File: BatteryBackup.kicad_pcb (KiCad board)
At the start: 2 copper layers, 49 x 32 mm, 16 parts, among them J1 Power, J2 Power, J3 PowerOut, Q1 FDMT800100DC, Q2 FDMT800100DC, U1 LTC4357DCB, U2 LTC4357DCB

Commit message: routet
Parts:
- moved R2 15.2 mm to (137.0, 70.7)
- moved C4 15.2 mm to (139.0, 70.8)
- moved R1 13.8 mm to (145.7, 82.7)
- moved C3 13.7 mm to (144.0, 82.7)
- moved U1 10.4 mm to (141.7, 86.4), turned to 90 degrees
- moved U2 8.81 mm to (141.7, 73.4), turned to 90 degrees
- moved Q1 1.50 mm to (148.5, 88.8), turned to 0 degrees
- moved Q2 0.50 mm to (148.0, 74.2), turned to 0 degrees
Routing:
- net /IdealDiode/Vout: track 0.00 -> 85.8 mm, vias 0 -> 2
- net /IdealDiode1/Vin: track 0.00 -> 13.1 mm
- net /IdealDiode/Vin: track 0.00 -> 12.1 mm
- net GND: track 0.00 -> 12.0 mm, vias 0 -> 9
- net Net-(U1-Vdd): track 0.00 -> 6.21 mm
- net Net-(Q2-G): track 0.00 -> 4.51 mm
- net Net-(U2-Vdd): track 0.00 -> 4.34 mm
- net Net-(Q1-G): track 0.00 -> 3.26 mm
- added copper zone on B.Cu, net GND

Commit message: cooling
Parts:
- moved R2 5.09 mm to (141.6, 68.5), turned to 180 degrees
- moved C4 2.64 mm to (141.5, 70.0), turned to 0 degrees
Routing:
- net /IdealDiode/Vout: track 85.8 -> 30.4 mm
- net Net-(U2-Vdd): track 4.34 -> 3.64 mm
- net GND: track 12.0 -> 12.5 mm, vias 9 -> 8
- added copper zone on F.Cu, net /IdealDiode/Vout

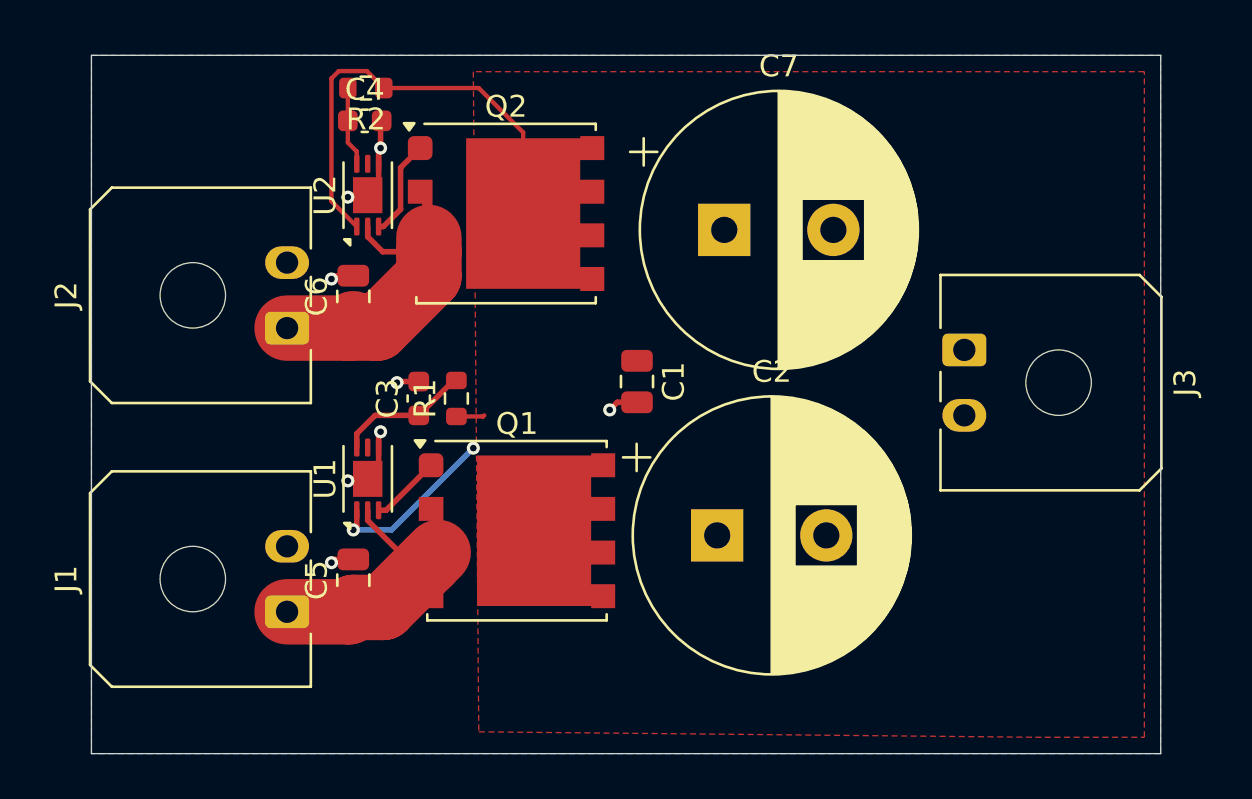
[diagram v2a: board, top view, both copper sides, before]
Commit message: skiftet til LTC4359
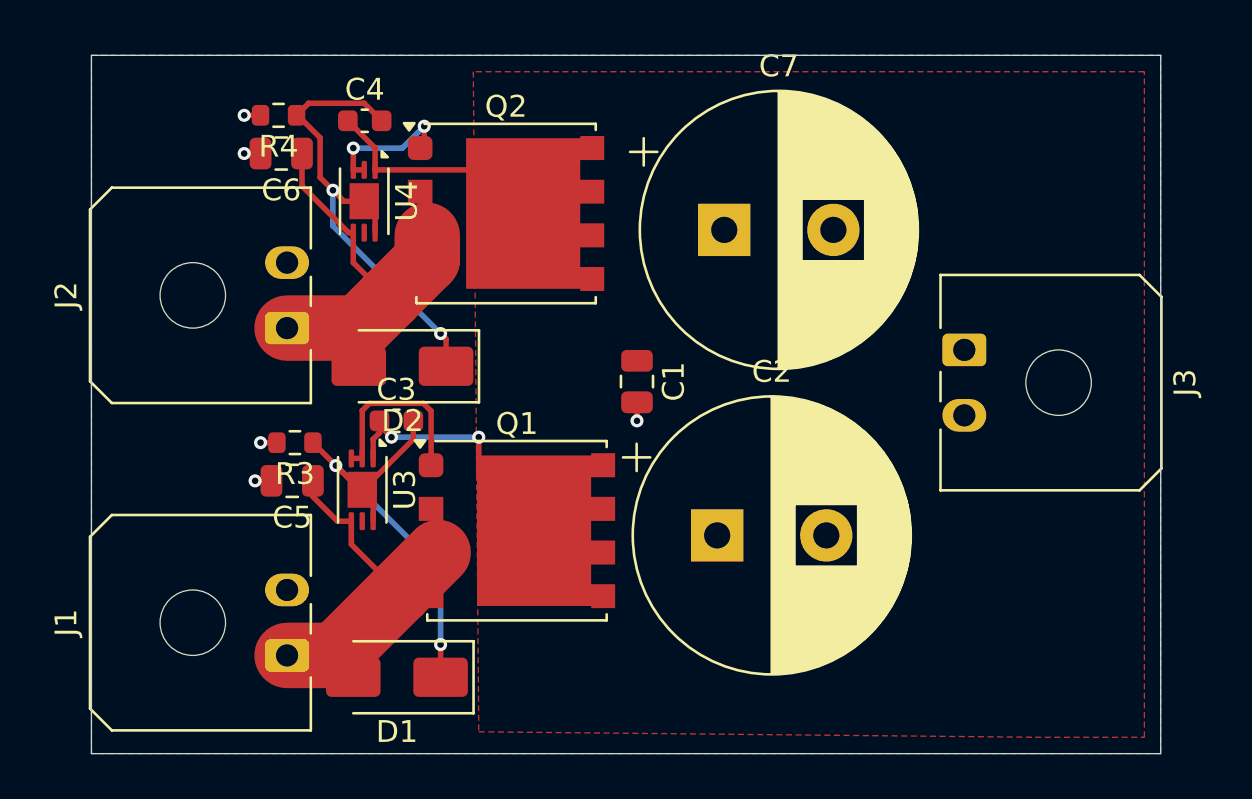
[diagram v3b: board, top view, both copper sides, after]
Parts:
- removed R1, R2: 100, Resistor_SMD:R_0603_1608Metric
- removed U1, U2: LTC4357DCB, Package_DFN_QFN:DFN-6-1EP_3x2mm_P0.5mm_EP1.65x1.35mm
- added D1: SMAJ24CA, Diode_SMD:D_SMA, F.Cu at (143.0, 95.5)
- added D2: SMAJ24CA, Diode_SMD:D_SMA, F.Cu at (143.2, 81.2)
- added R3: 1k, Resistor_SMD:R_0603_1608Metric, F.Cu at (138.3, 84.8)
- added R4: 1k, Resistor_SMD:R_0603_1608Metric, F.Cu at (137.6, 69.8)
- added U3: LTC4359-DCB, Package_DFN_QFN:DFN-6-1EP_3x2mm_P0.5mm_EP1.65x1.35mm, F.Cu at (141.4, 86.9)
- added U4: LTC4359-DCB, Package_DFN_QFN:DFN-6-1EP_3x2mm_P0.5mm_EP1.65x1.35mm, F.Cu at (141.5, 73.7)
- C3, C4: value 100n -> 1,5uF
- moved C6 7.33 mm to (137.7, 71.5), turned to 180 degrees
- moved C5 5.34 mm to (138.2, 86.5), turned to 180 degrees
- moved J1 2.00 mm to (138.0, 94.5)
- moved C3 1.45 mm to (143.0, 83.8), turned to 0 degrees
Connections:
- C3 pad 1: Net-(U1-Vdd) -> /IdealDiode/Vout
- C3 pad 2: GND -> Net-(D1-A1)
- C4 pad 1: Net-(U2-Vdd) -> /IdealDiode/Vout
- C4 pad 2: GND -> Net-(D2-A1)
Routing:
- net Net-(D2-A1): track 0.00 -> 22.1 mm, vias 0 -> 2
- net Net-(D1-A1): track 0.00 -> 20.6 mm, vias 0 -> 2
- net GND: track 12.5 -> 3.85 mm, vias 8 -> 5
- net /IdealDiode/Vout: track 30.4 -> 22.5 mm
- net Net-(U1-Vdd): track 6.21 -> 0.00 mm
- net Net-(Q1-G): track 3.26 -> 8.62 mm
- net /IdealDiode1/Vin: track 13.1 -> 17.2 mm
- net /IdealDiode/Vin: track 12.1 -> 16.0 mm
- net Net-(U2-Vdd): track 3.64 -> 0.00 mm
- net Net-(Q2-G): track 4.51 -> 6.24 mm, vias 0 -> 2

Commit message: fejlretning
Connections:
- U3 pad 3: Net-(Q1-G) -> /IdealDiode/Vin
- U4 pad 3: Net-(Q2-G) -> /IdealDiode1/Vin
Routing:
- net /IdealDiode/Vin: track 16.0 -> 19.8 mm, vias 0 -> 2
- net /IdealDiode1/Vin: track 17.2 -> 20.1 mm, vias 0 -> 2
- net Net-(Q2-G): track 6.24 -> 5.65 mm
- net Net-(Q1-G): track 8.62 -> 8.05 mm
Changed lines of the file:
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@@
 			(layers "F.Cu" "F.Mask" "F.Paste")
 			(roundrect_rratio 0.25)
-			(net 7 "Net-(Q1-G)")
+			(net 5 "/IdealDiode/Vin")
 			(pinfunction "SRC")
 			(pintype "input")
@@
 			(layers "F.Cu" "F.Mask" "F.Paste")
 			(roundrect_rratio 0.25)
-			(net 8 "Net-(Q2-G)")
+			(net 6 "/IdealDiode1/Vin")
 			(pinfunction "SRC")
 			(pintype "input")
@@
 	)
 	(segment
+		(start 140.91 85.41)
+		(end 140.5 85)
+		(width 0.2)
+		(layer "F.Cu")
+		(net 5)
+	)
+	(segment
 		(start 140.91 88.3475)
 		(end 140.91 89.41)
@@
 	)
 	(segment
-		(start 139.15 87.225)
+		(start 139.4625 87.5375)
 		(end 140.2725 88.3475)
 		(width 0.254)
@@
 	)
 	(segment
+		(start 140.91 85.4725)
+		(end 140.91 85.41)
+		(width 0.2)
+		(layer "F.Cu")
+		(net 5)
+	)
+	(segment
+		(start 139.15 87.225)
+		(end 139.4625 87.5375)
+		(width 0.254)
+		(layer "F.Cu")
+		(net 5)
+	)
+	(segment
 		(start 143.0875 91.5875)
 		(end 144.89 89.785)
@@
 		(net 5)
 	)
+	(via
+		(at 140.5 85)
+		(size 0.6)
+		(drill 0.3)
+		(layers "F.Cu" "B.Cu")
+		(net 5)
+	)
+	(via
+		(at 139.4625 87.5375)
+		(size 0.6)
+		(drill 0.3)
+		(layers "F.Cu" "B.Cu")
+		(net 5)
+	)
+	(segment
+		(start 140.150057 85)
+		(end 139.4625 85.687557)
+		(width 0.2)
+		(layer "B.Cu")
+		(net 5)
+	)
+	(segment
+		(start 139.4625 85.687557)
+		(end 139.4625 87.5375)
+		(width 0.2)
+		(layer "B.Cu")
+		(net 5)
+	)
+	(segment
+		(start 140.5 85)
+		(end 140.150057 85)
+		(width 0.2)
+		(layer "B.Cu")
+		(net 5)
+	)
 	(segment
 		(start 140.7815 75.125)
-		(end 138.65 72.9935)
+		(end 139.20325 73.54675)
 		(width 0.254)
 		(layer "F.Cu")
@@
 	)
 	(segment
+		(start 140.5 72.25)
+		(end 140.25 72)
+		(width 0.2)
+		(layer "F.Cu")
+		(net 6)
+	)
+	(segment
+		(start 141 72.25)
+		(end 140.5 72.25)
+		(width 0.2)
+		(layer "F.Cu")
+		(net 6)
+	)
+	(segment
 		(start 142.625 78.125)
 		(end 144.39 76.36)
@@
 	)
 	(segment
-		(start 138.65 72.9935)
-		(end 138.65 71.5)
+		(start 139.20325 73.54675)
+		(end 138.65 72.9935)
 		(width 0.254)
 		(layer "F.Cu")
@@
 	)
 	(segment
-		(start 144.210294 82.947)
-		(end 141.739706 82.947)
+		(start 138.65 72.9935)
+		(end 138.65 71.5)
 		(width 0.254)
 		(layer "F.Cu")
-		(net 7)
+		(net 6)
+	)
+	(via
+		(at 139.20325 73.54675)
+		(size 0.6)
+		(drill 0.3)
+		(layers "F.Cu" "B.Cu")
+		(net 6)
+	)
+	(via
+		(at 140.25 72)
+		(size 0.6)
+		(drill 0.3)
+		(layers "F.Cu" "B.Cu")
+		(net 6)
 	)
 	(segment
-		(start 144.565 83.301706)
-		(end 144.210294 82.947)
-		(width 0.254)
+		(start 139.20325 73.04675)
+		(end 139.20325 73.54675)
+		(width 0.2)
+		(layer "B.Cu")
+		(net 6)
+	)
+	(segment
+		(start 140.25 72)
+		(end 139.20325 73.04675)
+		(width 0.2)
+		(layer "B.Cu")
+		(net 6)
+	)
+	(segment
+		(start 141.41 85.4725)
+		(end 141.41 83.31489)
+		(width 0.2)
 		(layer "F.Cu")
 		(net 7)
 	)
 	(segment
-		(start 141.41 83.276706)
-		(end 141.41 85.4725)
-		(width 0.254)
+		(start 144.19911 82.974)
+		(end 144.565 83.33989)
+		(width 0.2)
 		(layer "F.Cu")
 		(net 7)
 	)
 	(segment
-		(start 140.91 85.4725)
-		(end 141.41 85.4725)
-		(width 0.254)
+		(start 141.41 83.31489)
+		(end 141.75089 82.974)
+		(width 0.2)
 		(layer "F.Cu")
 		(net 7)
 	)
 	(segment
-		(start 141.739706 82.947)
-		(end 141.41 83.276706)
-		(width 0.254)
+		(start 141.75089 82.974)
+		(end 144.19911 82.974)
+		(width 0.2)
 		(layer "F.Cu")
 		(net 7)
 	)
 	(segment
-		(start 144.565 85.785)
-		(end 144.565 83.301706)
-		(width 0.254)
+		(start 144.565 83.33989)
+		(end 144.565 85.785)
+		(width 0.2)
 		(layer "F.Cu")
 		(net 7)
 	)
 	(segment
-		(start 144.25 71.065)
-		(end 144.065 71.25)
-		(width 0.254)
+		(start 141.5 72.25)
+		(end 141.5 71.636712)
+		(width 0.2)
 		(layer "F.Cu")
 		(net 8)
 	)
 	(segment
-		(start 141 72.25)
-		(end 141 71.25)
-		(width 0.254)
+		(start 144.25 71.065)
+		(end 144.065 71.25)
+		(width 0.2)
 		(layer "F.Cu")
 		(net 8)
@@
 		(start 144.25 70.25)
 		(end 144.25 71.065)
-		(width 0.254)
+		(width 0.2)
 		(layer "F.Cu")
 		(net 8)
 	)
 	(segment
-		(start 141.5 72.25)
-		(end 141 72.25)
-		(width 0.254)
+		(start 141.5 71.636712)
+		(end 141.181644 71.318356)
+		(width 0.2)
 		(layer "F.Cu")
 		(net 8)
@@
 	)
 	(via
-		(at 141 71.25)
+		(at 141.181644 71.318356)
 		(size 0.6)
 		(drill 0.3)
@@
 	)
 	(segment
-		(start 141 71.25)
-		(end 143.25 71.25)
-		(width 0.254)
+		(start 143.181644 71.318356)
+		(end 144.25 70.25)
+		(width 0.2)
 		(layer "B.Cu")
 		(net 8)
 	)
 	(segment
-		(start 143.25 71.25)
-		(end 144.25 70.25)
-		(width 0.254)
+		(start 141.181644 71.318356)
+		(end 143.181644 71.318356)
+		(width 0.2)
 		(layer "B.Cu")
 		(net 8)
